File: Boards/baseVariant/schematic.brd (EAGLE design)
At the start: 160 x 100 mm, 116 parts, among them IC1 BQ24120

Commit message: normal Push.
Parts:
- removed 3V3: TPSB2,54, testpad:B2,54
- removed BAT: (no value), SparkFun-Connectors:1X03
- removed C63, C64: 220uf, adafruit:PANASONIC_D
- removed D5, D7: SMA, SparkFun:SMA-DIODE
- removed D6: 5320, SparkFun:SMA-DIODE
- removed L3: 10uH, SparkFun-Passives:B82462G
- removed L4: 47uh, BaseApp:INDUCTOR-10X9.8X6
- removed LED4, LED6: (no value), led:CHIP-LED0603
- removed LM2596: (no value), BaseApp:TO-263-6(5LEADS+1TAB)
- removed R11, R12, R20, R7: 7.5k, SparkFun-Passives:0402-RES
- removed R13, R52: 3.1K, BaseApp:R0603
- removed R3, R6: 1.5k, SparkFun-Passives:0402-RES
- removed R58: 1K, BaseApp:R0603
- removed RSNS: 0.1, SparkFun-Passives:0402-RES
- removed RST_BRD: (no value), SparkFun-Connectors:MOLEX-1X2
- added C18, C19: 4.7uF, rcl:C0603
- added C2: 200uF, schematic:PANASONIC_E
- added CN1: (no value), adafruit:DCJACK_2MM_PTH
- added CN2: (no value), adafruit:JST-PH-2-THM
- added D3: DIODE-SCHOTTKY_, schematic:SMA-DIODE
- added GND, VCC: TPSB2,54, testpad:B2,54
- added J1: MAX9850ETI+, schematic:21-0140L_T2855-3
- added L1: 33uH 3A, schematic:INDUCTOR-10X9.8X6
- added Q1, Q2, Q3, Q4, Q5: BSS84, transistor-small-signal:SOT23
- added U$1: (no value), schematic:5PIN_SOT23
- C15: value 150pf/50V -> 3.3nF
- C16: value 3.3nf/50v -> 150pF
- C3: value 0.1uF -> 680uF; device SparkFun-Capacitors:0402-CAP -> schematic:PANASONIC_E
- C4: value 0.1uF -> 220uF; device SparkFun-Capacitors:0402-CAP -> schematic:PANASONIC_E
- C7: device adafruit:E2,5-6 -> adafruit:PANASONIC_F
- C8: value 10uF -> 4.7uF; device SparkFun-Capacitors:0402-CAP -> rcl:C0603
- IC1: value BQ24120 -> LM2596S; device texas:QFN20_3,5X4,5 -> national-semiconductor:TO263-5
- ICSP: value PIC-ICSPPOLAR_LOCK -> PIC-ICSPPTH; device SparkFun-Connectors:MOLEX-1X6_LOCK -> SparkFun-Connectors:MOLEX-1X6
- LED3: device led:CHIP-LED0603 -> schematic:CHIP-LED0603
- R1: value 1K -> (none); device BaseApp:R0603 -> SparkFun-Passives:0402-RES
- R15: value 51R -> 45.3
- R19: value 20K -> 49.9k
- R2: value 1.5k -> 2k
- moved C8 181.5 mm to (39.4, 22.9), turned to 90 degrees
- moved LED3 176.2 mm to (39.4, 85.1)
- moved R2 173.2 mm to (47.0, 11.4)
- moved C4 164.0 mm to (27.9, 43.2), turned to 90 degrees
- moved R1 138.8 mm to (41.9, 85.1), turned to 270 degrees
- moved C3 135.3 mm to (6.35, 19.1)
- moved JP4 134.2 mm to (27.9, 1.27)
- moved R22 131.1 mm to (49.5, 20.3), turned to 270 degrees
- moved MCP1826 126.0 mm to (44.5, 22.9)
- moved C13 124.0 mm to (49.5, 24.1), turned to 90 degrees
- moved IC1 120.8 mm to (8.89, 30.5), turned to 90 degrees
- moved U$6 110.5 mm to (82.5, 15.2)
- moved U$15 108.0 mm to (59.7, 15.2)
- moved C7 103.9 mm to (53.3, 29.2), turned to 270 degrees
- moved VDD 5.08 mm to (-71.1, 82.5)
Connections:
- net +48V renamed +57
- removed net 22.2V: D5.A
- removed net N$17: C16.2, C17.2, U$4.15
- removed net N$28: LED6.A, R6.1
- removed net N$29: LED4.A, R3.1
- removed net N$31: MCP1826.2
- removed net N$34: C15.2, C16.1, R21.1
- removed net N$40: IC1.8, R7.2
- removed net N$44: D6.C, L4.P$2, LM2596.2
- removed net N$46: BAT.1, IC1.14, RSNS.1
- removed net N$61: LM2596.4, R1.2, R13.1
- removed net N$90: R52.1, R58.2, RST_BRD.2
- removed net NTC: BAT.2, IC1.12, R12.2, R20.1
- removed net VIN: C63.+, D5.C, D7.C, LM2596.1, R52.2
- removed net VTSB: C4.1, IC1.11, R12.1
- new net AVDD: J1.17
- new net CRGH_STAT: R1.2, U$1.P$1
- new net DGND: J1.6
- new net DVDD: J1.4
- new net N$27: R2.1, U$1.P$5
- new net PD_VDC: Q1.3
- new net PGND: J1.24
- new net PVDC: C4.+, IC1.4, L1.P$2, Q2.3
- new net PVDD: J1.26
- new net SVSS: J1.20
- new net VCC: C2.+, LED3.A, Q1.2, Q2.2, Q3.2, Q5.3, U$1.P$4, VCC.TP
- new net VSOURCE: C18.1, MCP1826.2, Q4.2, Q5.2
- net +3V3: no longer 3V3.TP, C64.+, L4.P$1, R13.2, R14.1, R4.1, R5.1
- net 25V: no longer D7.A
- net AGND: now also J1.14
- net GND: now also C18.2, C19.2, C2.-, C3.-, C4.-, CN2.2, D3.A, GND.TP, IC1.3, IC1.5, Q1.1, Q2.1, Q3.1, Q4.1, Q5.1, R2.2, U$1.P$2; no longer BAT.3, C3.2, C4.2, C63.-, C64.-, D6.A, IC1.10, IC1.16, IC1.17, IC1.18, LM2596.3, LM2596.5, LM2596.6, R1.1, R11.1, R20.2, R58.1, R7.1, RST_BRD.1
- net N$13: no longer R21.2
- net N$14: now also CN1.GND; no longer C3.1, IC1.7
- net N$2: now also D3.C, IC1.2, L1.P$1; no longer IC1.1, IC1.20, L3.P$1
- net N$30: now also C3.+, CN1.PWR, IC1.1; no longer LED3.A, R2.1
- net N$36: now also LED3.C, R1.1; no longer IC1.9, R11.2
- net N$5: now also CN1.GNDBREAK; no longer IC1.19, LED4.C
- net N$6: now also C16.2, C17.2, R21.1, U$4.15; no longer IC1.5, LED6.C
- net N$7: now also C15.2, C16.1, R21.2; no longer IC1.2, LED3.C
- net VBAT: now also C19.1, CN2.1, Q4.3, U$1.P$3; no longer IC1.15, L3.P$2, RSNS.2
- net VBUS: now also Q3.3; no longer IC1.3, IC1.4, IC1.6, R2.2, R3.2, R6.2
- net VDD: now also R14.1, R4.1, R5.1
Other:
- board size 160 x 100 mm -> 101.6 x 88.6 mm

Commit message: Normal Push
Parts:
- removed Q1, Q3: BSS84, transistor-small-signal:SOT23
- added B1: DBLS201G, rectifier:DBS
- added D4, D5: BA340A, SparkFun-DiscreteSemi:SMA-DIODE
- moved Q2 128.6 mm to (-97.8, -20.3), turned to 0 degrees
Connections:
- removed net N$14: CN1.GND
- removed net N$30: C3.+, CN1.PWR, IC1.1
- removed net N$5: CN1.GNDBREAK
- new net N$17: B1.AC1, CN1.PWR
- new net N$31: B1.+, C3.+, IC1.1
- new net OR_VDC: C2.+, D4.C, D5.C
- net GND: now also B1.-, B1.AC2, CN1.GND, CN1.GNDBREAK; no longer Q1.1, Q2.1, Q3.1
- net PD_VDC: now also D4.A; no longer Q1.3
- net PVDC: now also D5.A; no longer Q2.3
- net VBUS: no longer Q3.3
- net VCC: no longer C2.+, Q1.2, Q2.2, Q3.2

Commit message: normal Push.
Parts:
- removed C91, C92: 0.1uf, BaseApp:C0603
- removed C93: 1uf, BaseApp:C0603
- removed C94: 0.1uf/100V, BaseApp:C0603
- removed LED5: (no value), adafruit:CHIP-LED0603
- removed Q2, Q4, Q5: BSS84, transistor-small-signal:SOT23
- removed R49: 330R, BaseApp:R0603
- removed R50: 7.15K, BaseApp:R0603
- removed SMAJ58A: (no value), BaseApp:SCHOTTKY_SMA
- removed U$14: LTC4263, BaseApp:SOIC-14
- added C20, C21: 0.1uf, rcl:C0603
- added D6, D7: BA340A, SparkFun-DiscreteSemi:SMA-DIODE
- added LED4: (no value), led:CHIP-LED0603
- added Q1: BSS84, transistor-small-signal:SOT23
- added R11, R12, R6, R7: 57.6k, resistor:R0402
- added R13: 10k, resistor:R0402
- added R20: 71.5, resistor:R0402
- added R3: (no value), SparkFun-Passives:0402-RES
- C18, C8: value 4.7uF -> 0.1uf
- LED3: device schematic:CHIP-LED0603 -> led:CHIP-LED0603
- R1: value (none) -> 57.6k; device SparkFun-Passives:0402-RES -> resistor:R0402
- R2: value 2k -> (none)
- U$1: value (none) -> AAT3672-1/-2; device schematic:5PIN_SOT23 -> schematic:AAT3672-1/-2
- moved B1 242.8 mm to (147.3, -12.7), turned to 90 degrees
- moved D5 236.6 mm to (138.4, -16.5), turned to 90 degrees
- moved D4 232.6 mm to (134.6, -16.5), turned to 90 degrees
- moved GND 221.0 mm to (121.9, -17.8), turned to 90 degrees
- moved J1 211.0 mm to (114.3, -15.2), turned to 90 degrees
- moved LED3 197.6 mm to (-104.1, -50.8)
- moved R2 155.5 mm to (-99.1, -41.9)
- moved C8 154.5 mm to (-99.1, -45.7), turned to 0 degrees
- moved C18 148.8 mm to (-99.1, -50.8), turned to 0 degrees
- moved R1 144.5 mm to (158.8, 0.00), turned to 90 degrees
- moved C13 113.7 mm to (160.0, 50.8)
- moved C2 113.7 mm to (142.2, 45.7)
- moved C3 113.7 mm to (116.8, 45.7)
- moved C4 113.7 mm to (138.4, 69.8)
- moved C7 113.7 mm to (163.8, 55.9)
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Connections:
- removed net 25V: C28.+, R17.1, R18.2, U$28.P$2
- removed net CRGH_STAT: R1.2, U$1.P$1
- removed net N$27: R2.1, U$1.P$5
- removed net N$31: B1.+, C3.+, IC1.1
- removed net N$92: LED5.C, R49.1
- removed net N$93: R49.2, U$14.1
- removed net N$94: C93.2, R50.1, U$14.4
- removed net OR_VDC: C2.+, D4.C, D5.C
- removed net PVDC: C4.+, D5.A, IC1.4, L1.P$2
- new net CHRADP: R11.2, R12.1, U$1.P$10
- new net N$14: C20.2, U$1.P$14
- new net N$28: R7.1, U$1.P$6
- new net N$42: C21.2, U$1.P$15
- new net N$47: LED4.C, R7.2
- new net N$48: LED3.C, R6.2
- new net N$49: LED3.A
- new net N$5: R1.2, U$1.P$2
- new net N$50: LED4.A
- new net PAS_VDC: D5.A, U$6.4, U$6.5
- new net TS: R13.1, U$1.P$12
- new net VIN: C2.+, C3.+, D4.C, D5.C, D6.C, IC1.1, R3.2
- new net VJACK: B1.+, D6.A
- new net VOUT: C4.+, D7.A, IC1.4, L1.P$2, Q1.1, R2.1
- net +57: no longer C92.2, C94.2, LED5.A, SMAJ58A.C, U$14.11, U$6.4, U$6.5
- net AGND: no longer C91.1, C92.1, C93.1, C94.1, R50.2, SMAJ58A.A, U$14.10, U$14.2, U$14.5, U$14.6, U$14.7, U$14.9, U$6.7, U$6.8
- net GND: now also C20.1, C21.1, R1.1, R12.2, R20.1, R3.1, U$1.P$1, U$1.P$5, U$6.7, U$6.8; no longer Q4.1, Q5.1, U$1.P$2
- net N$22: now also R6.1, U$1.P$4; no longer C91.2, U$14.12, U$14.13, U$14.14, U$14.3
- net N$36: now also R20.2, U$1.P$11; no longer LED3.C, R1.1
- net PD_VDC: now also C28.+, R17.1, R18.2, U$28.P$2
- net VBAT: now also U$1.P$13, U$1.P$9; no longer C8.1, Q4.3, U$1.P$3
- net VBUS: now also Q1.3
- net VCC: no longer LED3.A, Q5.3, U$1.P$4
- net VSOURCE: now also C8.1, D7.C, Q1.2, R11.1, R13.2, U$1.P$3, U$1.P$7, U$1.P$8; no longer Q4.2, Q5.2
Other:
- board size 101.6 x 88.6 mm -> 69.8 x 69.9 mm

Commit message: normal Push
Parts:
- removed C14: 0.47u, BaseApp:C0603
- removed C5, C6, C9: (no value), BaseApp:C0603
- removed C65, C66, C96, C97: 0.1uf, BaseApp:C0603
- removed D2: BAT54, diode:SOT23
- removed DUO-LED2: (no value), BaseApp:DUOLED-C-0603
- removed FID1, FID2, FID3, FID4: FIDUCIAL1X2.5, SparkFun-Aesthetics:FIDUCIAL-1X2.5
- removed FX1, FX2: TG110-E055N5, halo-electronics:N5
- removed GND, VCC, VDD: TPSB2,54, testpad:B2,54
- removed ICSP: PIC-ICSPPTH, SparkFun-Connectors:MOLEX-1X6
- removed J1: MAX9850ETI+, schematic:21-0140L_T2855-3
- removed JP1: (no value), SparkFun-Passives:SJ_2S
- removed P-RESET: SPST_TACT-EVQQ2, adafruit:EVQ-Q2
- removed PIC25K50: PIC18F25K50, BaseApp:SOIC-28
- removed POWER: (no value), switch-omron:B3F-31XX
- removed R10: ~200R, BaseApp:R0603
- removed R14: 300K, rcl:R0603
- removed R28, R9: 10K, BaseApp:R0603
- removed R4, R5: 330R, rcl:R0603
- removed R42, R43, R56, R57: 75R, BaseApp:R0603
- removed U$15, U$6: RJ45, BaseApp:RJ-45-NOMAGNETICS_BI-LED
- removed U$18: LIGHT_PIPE, BaseApp:LIGHT-PIPE
- added LED5, LED6: (no value), led:LED3MM
- added U$2: ATMEGA32U4QFN, SparkFun-DigitalIC:QFN-44
- added U1, U2: MAGJACK-POE, SparkFun-Connectors:MAGJACK-POE
- added USB1: USB_SHIELDUSB_A_VERTICAL, schematic:USB_A_VERTICAL_PTH
- LED1, LED2: device adafruit:CHIP-LED0603 -> led:LED3MM
- moved R7 232.2 mm to (87.1, 63.1), turned to 90 degrees
- moved R6 231.2 mm to (89.0, 63.1), turned to 90 degrees
- moved LED4 228.8 mm to (86.9, 66.9), turned to 180 degrees
- moved LED3 226.1 mm to (88.8, 66.9), turned to 180 degrees
- moved R13 221.5 mm to (67.0, 58.0), turned to 270 degrees
- moved C8 202.1 mm to (80.0, 48.0), turned to 270 degrees
- moved C21 198.6 mm to (65.0, 9.00)
- moved C20 195.3 mm to (65.0, 7.00), turned to 180 degrees
- moved D7 194.8 mm to (77.0, 48.0), turned to 90 degrees
- moved R20 194.4 mm to (56.0, 11.0), turned to 270 degrees
- moved R2 187.9 mm to (67.0, 46.0), turned to 180 degrees
- moved Q1 187.2 mm to (72.0, 47.0), turned to 90 degrees
- moved R12 186.3 mm to (58.0, 11.0), turned to 90 degrees
- moved R11 180.5 mm to (54.0, 11.0), turned to 270 degrees
- moved C18 173.4 mm to (61.0, 16.0), turned to 90 degrees
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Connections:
- removed net !SHDN: PIC25K50.26
- removed net +3V3: R48.2
- removed net AGND: C1.1, J1.14, R15.2, U$4.9, U$4.PAD
- removed net AVDD: J1.17
- removed net DGND: J1.6
- removed net DVDD: J1.4
- removed net LED1: LED1.C, PIC25K50.24
- removed net LED2: LED2.C, PIC25K50.23
- removed net MCLR: ICSP.6, P-RESET.A, P-RESET.A', PIC25K50.1, R10.1
- removed net N$19: FX1.16, U$6.3
- removed net N$21: FX1.14, U$6.6
- removed net N$32: C96.2, R56.2
- removed net N$35: C6.2, JP1.1
- removed net N$37: JP1.2, R10.2, R9.1
- removed net N$38: C14.2, PIC25K50.14
- removed net N$49: LED3.A
- removed net N$50: LED4.A
- removed net N$69: C65.2, R42.2
- removed net N$70: C66.2, R43.2
- removed net N$73: FX2.15, R43.1
- removed net N$74: FX2.10, R42.1
- removed net N$75: FX1.11, U$6.1
- removed net N$77: FX1.9, U$6.2
- removed net N$78: R47.1, U$6.10
- removed net N$79: R48.1, U$6.11
- removed net N$80: FX2.16, U$15.3
- removed net N$87: FX2.14, U$15.6
- removed net N$88: FX2.11, U$15.1
- removed net N$89: FX2.9, U$15.2
- removed net N$91: R53.1, U$15.10
- removed net P-RX: PIC25K50.18
- removed net P-TX: D2.1, R14.2
- removed net P-TX*: D2.3, PIC25K50.17
- removed net PGC: ICSP.2, PIC25K50.27
- removed net PGD: ICSP.3, PIC25K50.28
- removed net PGND: J1.24
- removed net PVDD: J1.26
- removed net RA0: PIC25K50.2
- removed net RA1: PIC25K50.3
- removed net RB0: PIC25K50.21, POWER.2, R28.1
- removed net STAT: PIC25K50.25
- removed net SVSS: J1.20
- removed net VCC: VCC.TP
- new net N$17: USB1.3
- new net N$27: USB1.4
- new net N$29: USB1.P$3
- new net N$31: R47.1, U2.12
- net +2V: now also U1.3, U1.4, U2.3, U2.4; no longer FX1.2, FX1.7, FX2.2, FX2.7
- net ETH0_GRN-: now also U1.14; no longer U$15.12
- net GND: now also C1.1, R15.2, U$4.9, U$4.PAD, U1.GND0, U1.GND1, U2.10, U2.14, U2.GND0, U2.GND1; no longer C14.1, C5.2, C6.1, C65.1, C66.1, C9.2, C96.1, C97.1, GND.TP, ICSP.4, P-RESET.B, P-RESET.B', PIC25K50.19, PIC25K50.8, POWER.1, U$15.P$13, U$15.P$14, U$6.12, U$6.7, U$6.8, U$6.P$13, U$6.P$14
- net LAN_TX+: now also U1.5; no longer FX2.1
- net LAN_TX-: now also U1.6; no longer FX2.3
- net LAN_YLW: now also U1.11; no longer U$15.9
- net N$23: now also U2.11; no longer FX1.15, R57.1
- net N$24: now also R53.1, U1.12; no longer FX1.10, R56.1
- net N$25: now also R48.1, U2.13; no longer C97.2, R57.2
- net N$3: now also USB1.1; no longer LED1.A, R4.2
- net N$4: now also USB1.2; no longer LED2.A, R5.2
- net N$95: now also U1.13; no longer U$15.11
- net PAS_VDC: now also U2.9; no longer U$6.4, U$6.5
- net SP1: now also U1.10; no longer U$15.7, U$15.8
- net SP2: now also U1.9; no longer U$15.4, U$15.5
- net USB_D_N: no longer PIC25K50.15
- net USB_D_P: no longer PIC25K50.16
- net VDD: now also R48.2; no longer C5.1, C9.1, ICSP.5, PIC25K50.20, R14.1, R28.2, R4.1, R5.1, R9.2, VDD.TP
- net VSOURCE: now also LED3.A, LED4.A
- net WAN_RX+: now also U1.1, U2.1; no longer FX1.6, FX2.6
- net WAN_RX-: now also U1.2, U2.2; no longer FX1.8, FX2.8
- net WAN_TX+: now also U2.5; no longer FX1.1
- net WAN_TX-: now also U2.6; no longer FX1.3
- net WAN_YLW: no longer U$6.9
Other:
- board size 69.8 x 69.9 mm -> 93 x 70 mm

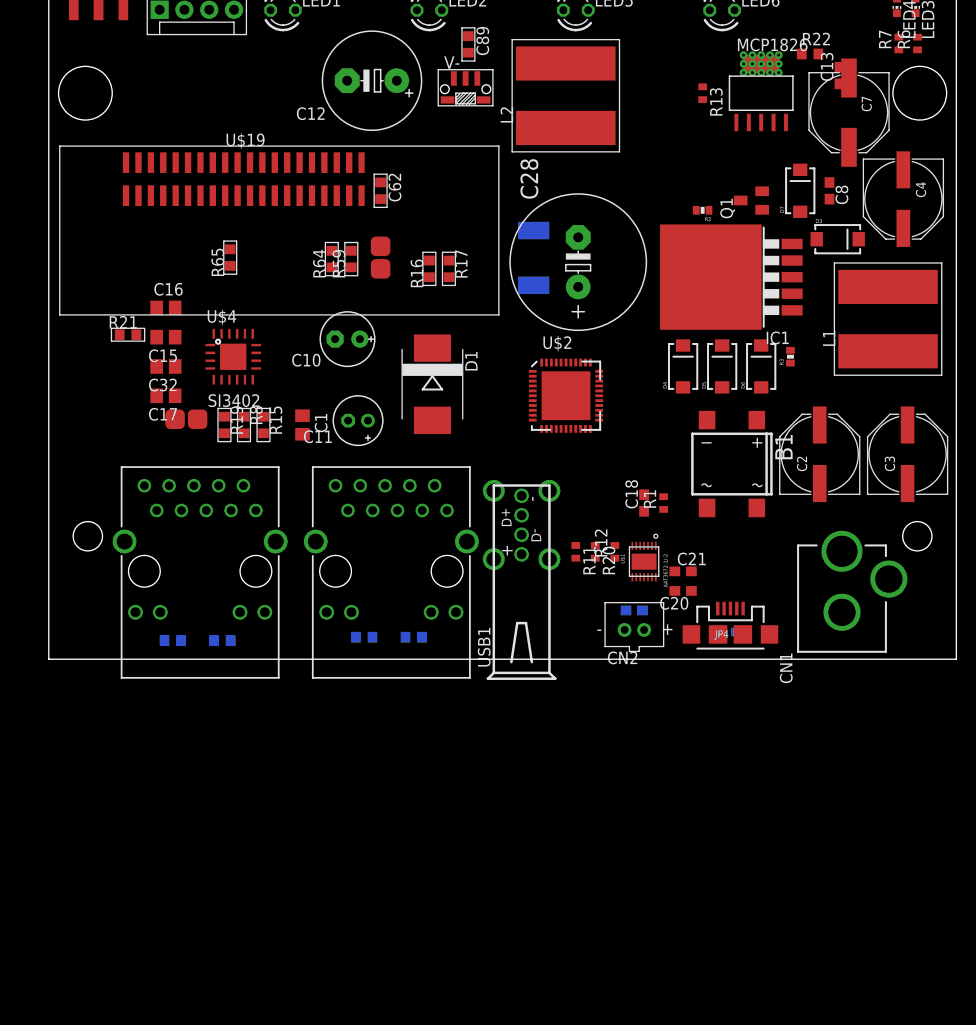
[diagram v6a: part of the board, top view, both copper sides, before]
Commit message: Normal Push, With Surge Protection on Host USB.
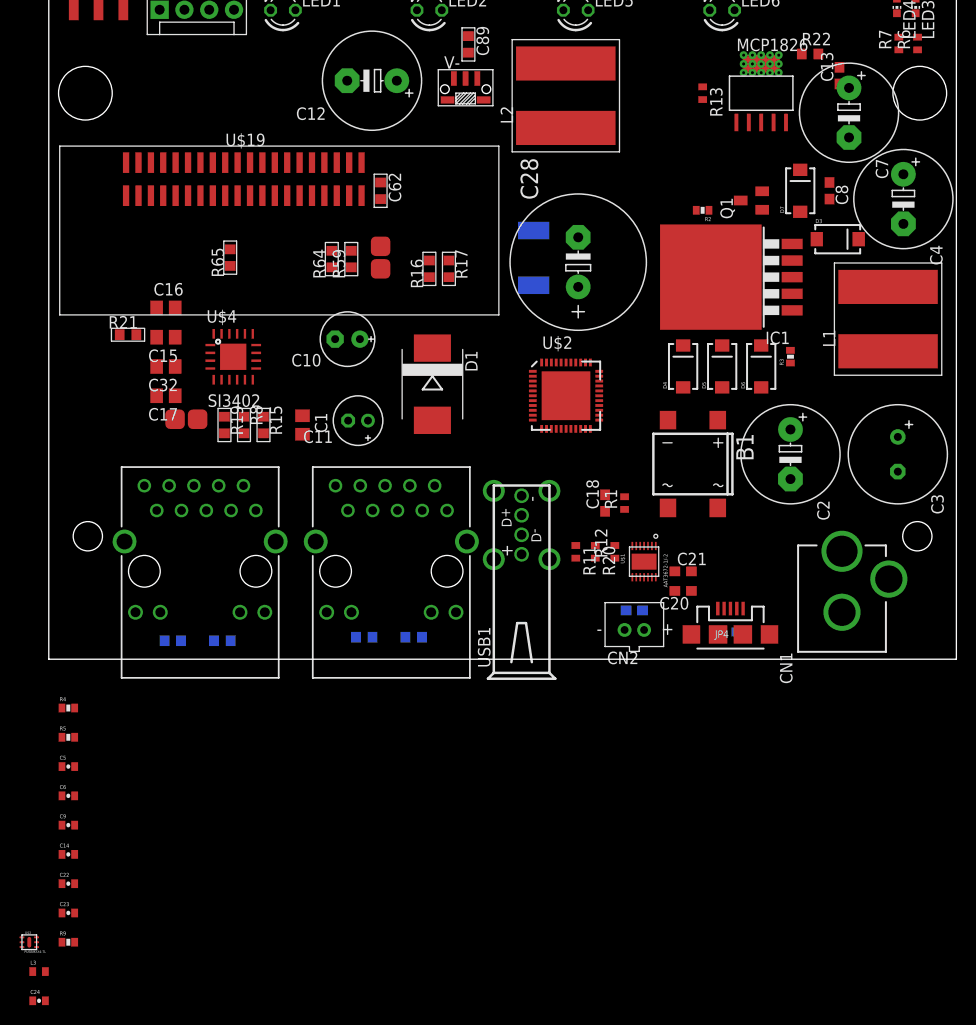
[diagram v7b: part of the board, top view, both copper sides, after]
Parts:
- added C14, C22, C5, C6, C9: (no value), SparkFun:0402-CAP
- added C23: 1uF, SparkFun:0402-CAP
- added C24: 0.1uF, SparkFun-Capacitors:0402-CAP
- added L3: (no value), SparkFun-Passives:C0402
- added R4, R5: 22, SparkFun:0402-RES
- added R9: 1k, SparkFun:0402-RES
- added U$3: PUSBMXX4-TL, schematic:PUSBMXX4-TL
- C2, C4: device schematic:PANASONIC_E -> schematic:E5-10,5
- C3: device schematic:PANASONIC_E -> schematic:E3,5-10
- C7: device adafruit:PANASONIC_F -> adafruit:E5-10,5
- moved B1 4.00 mm to (66.0, 20.0)
- moved C18 4.00 mm to (57.0, 16.0)
- moved R1 4.00 mm to (59.0, 16.0)
- moved C2 3.00 mm to (76.0, 21.0), turned to 270 degrees
- moved C3 1.00 mm to (87.0, 21.0), turned to 270 degrees
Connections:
- removed net N$17: USB1.3
- removed net N$27: USB1.4
- removed net N$29: USB1.P$3
- removed net N$3: USB1.1
- removed net N$4: USB1.2
- removed net VOUT: C4.+, D7.A, IC1.4, L1.P$2, Q1.1, R2.1
- new net N$19: U$2.13
- new net N$32: U$3.P$3
- new net N$33: U$3.P$4
- new net N$34: U$3.P$5
- new net N$37: C23.2, U$2.6
- new net N$38: R4.2, U$2.4
- new net N$39: R5.2, U$2.3
- new net N$41: L3.1, USB1.P$3
- new net N$43: R9.2, U$2.33
- new net VCC: C14.1, C22.1, C24.1, C4.+, C5.1, C6.1, C9.1, D7.A, IC1.4, L1.P$2, Q1.1, R2.1, U$2.14, U$2.24, U$2.34, U$2.42, U$2.44, U$3.P$6, USB1.1
- net GND: now also C14.2, C22.2, C23.1, C24.2, C5.2, C6.2, C9.2, L3.2, R9.1, U$2.15, U$2.23, U$2.35, U$2.43, U$2.5, U$3.P$7, USB1.4
- net USBUPD1_N: now also U$3.P$1, USB1.2
- net USBUPD1_P: now also U$3.P$2, USB1.3
- net USB_D_N: now also R5.1
- net USB_D_P: now also R4.1
- net VBUS: now also U$2.2, U$2.7

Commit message: Normal Push.
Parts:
- removed R59: (no value), BaseApp:R0603
- removed SKW71_UART: (no value), SparkFun-Connectors:1X03_SMD_RA_MALE
- added C25: 1uF, SparkFun:0402-CAP
- added J1: AVR_SPI_PRG_6NS, Sensor Mesh:2X3-NS
- added JP1: (no value), SparkFun-Connectors:STEREOJACK2.5MM
- added R10: 1k, SparkFun:0402-RES
- added R14, R23, R24, R25: 22, SparkFun:0402-RES
- added U$5: MAX5556ESA+, schematic:SO-8
- C2: value 200uF -> 1uF; device schematic:E5-10,5 -> SparkFun:0402-CAP
- moved R9 77.8 mm to (49.2, 32.9)
- moved C22 75.4 mm to (59.7, 25.6), turned to 90 degrees
- moved L3 74.6 mm to (56.7, 15.3), flipped to the bottom, turned to 270 degrees
- moved C9 73.7 mm to (56.6, 32.5), turned to 90 degrees
- moved C23 73.4 mm to (59.2, 20.0), turned to 90 degrees
- moved C24 72.5 mm to (45.5, 20.6), flipped to the bottom, turned to 90 degrees
- moved U$3 68.1 mm to (51.0, 13.8), flipped to the bottom, turned to 180 degrees
- moved C14 65.2 mm to (45.2, 28.8), turned to 270 degrees
- moved R5 61.0 mm to (56.2, 20.0), turned to 90 degrees
- moved R4 60.8 mm to (57.4, 20.0), turned to 90 degrees
- moved C6 57.6 mm to (45.5, 23.8), turned to 180 degrees
- moved C5 56.7 mm to (45.5, 25.3), turned to 180 degrees
- moved C2 18.9 mm to (61.6, 8.84), flipped to the bottom
- moved CN2 13.7 mm to (70.8, 11.5), turned to 90 degrees
- moved B1 11.3 mm to (77.3, 20.3)
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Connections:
- removed net N$19: U$2.13
- removed net SKW71_RX: SKW71_UART.1, U$19.37
- removed net SKW71_TX: SKW71_UART.2, U$19.38
- new net AT_RESET: J1.5, R10.1, U$2.13
- new net GPIO_18: U$19.13, U$5.2
- new net GPIO_20: U$19.11, U$5.1
- new net N$27: R14.2, R23.2
- new net N$35: R24.2, R25.2
- new net N$49: C2.2, JP1.4, R14.1
- new net N$51: C25.2, JP1.1, R24.1
- new net OUTL: C25.1, R25.1, U$5.8
- new net OUTR: C2.1, R23.1, U$5.5
- new net PB1/SCK: J1.3, U$2.9
- new net PB2/MOSI: J1.4, U$2.10
- new net PB3/MISO: J1.1, U$2.11
- new net PD2/RXD: U$19.38, U$2.20
- new net PD3/TXD: U$19.37, U$2.21
- net GND: now also J1.6, JP1.5, U$5.6; no longer C2.-, SKW71_UART.3
- net GPIO_19: now also U$5.3; no longer R59.2
- net GPIO_21: now also U$5.4
- net VCC: now also J1.2, R10.2, U$5.7
- net VDD: no longer R59.1
- net VIN: no longer C2.+
